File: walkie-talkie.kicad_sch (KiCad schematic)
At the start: 12 parts, among them J1 I2C, SW1 POWER, SW2 Transmit, U2 adafruit-MAX98357, U3 mems-mic

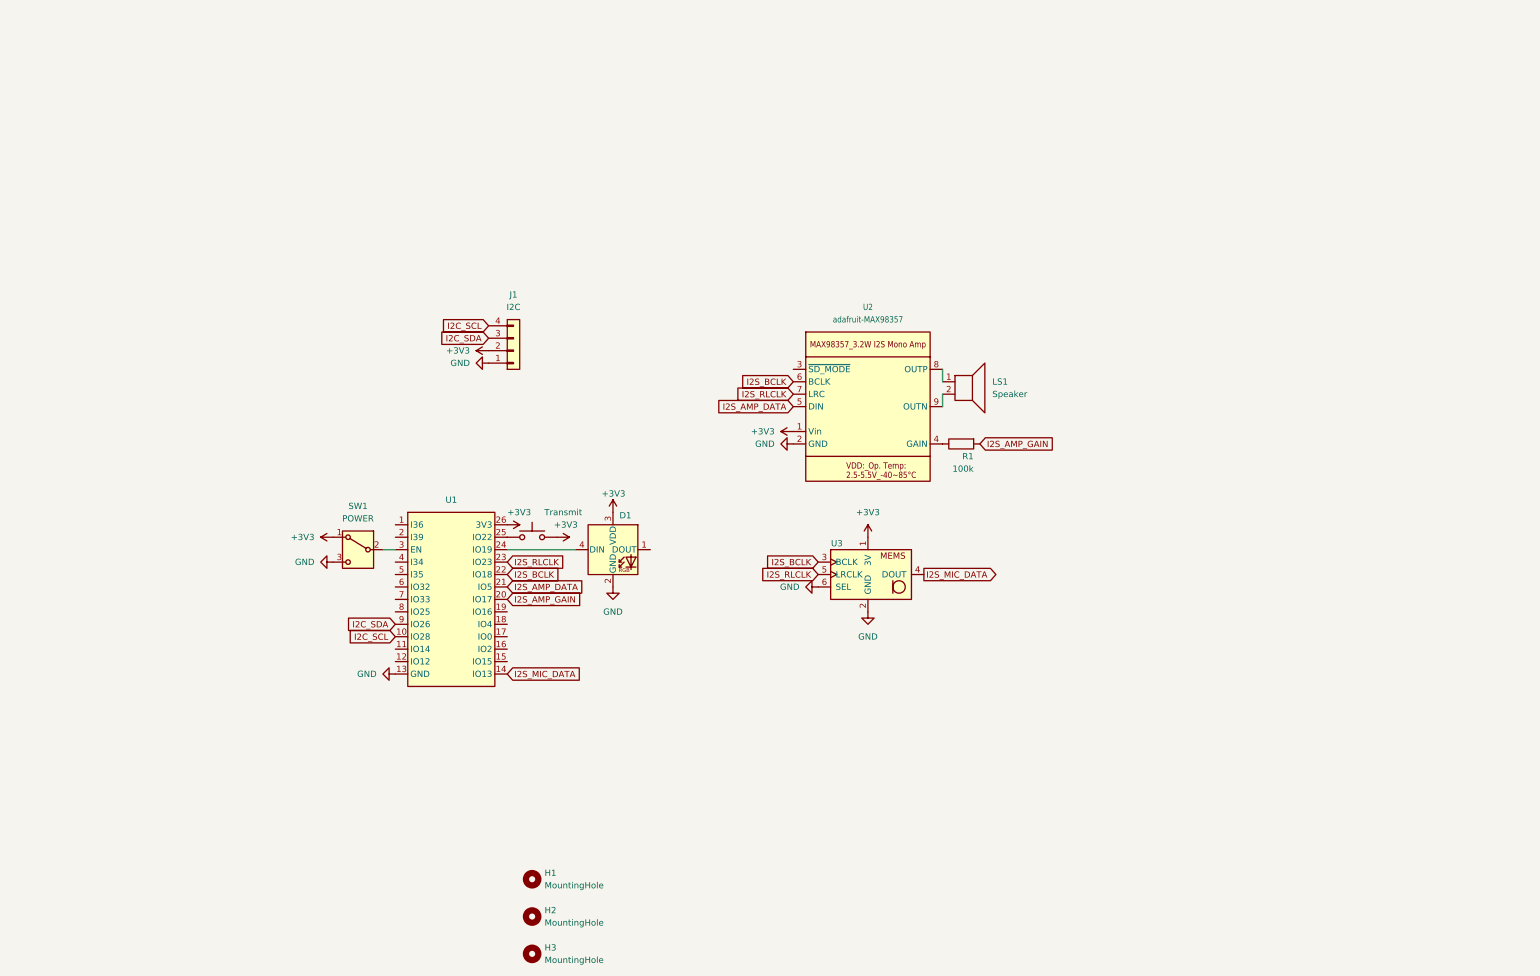
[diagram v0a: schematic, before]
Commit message: Add components for new PCB
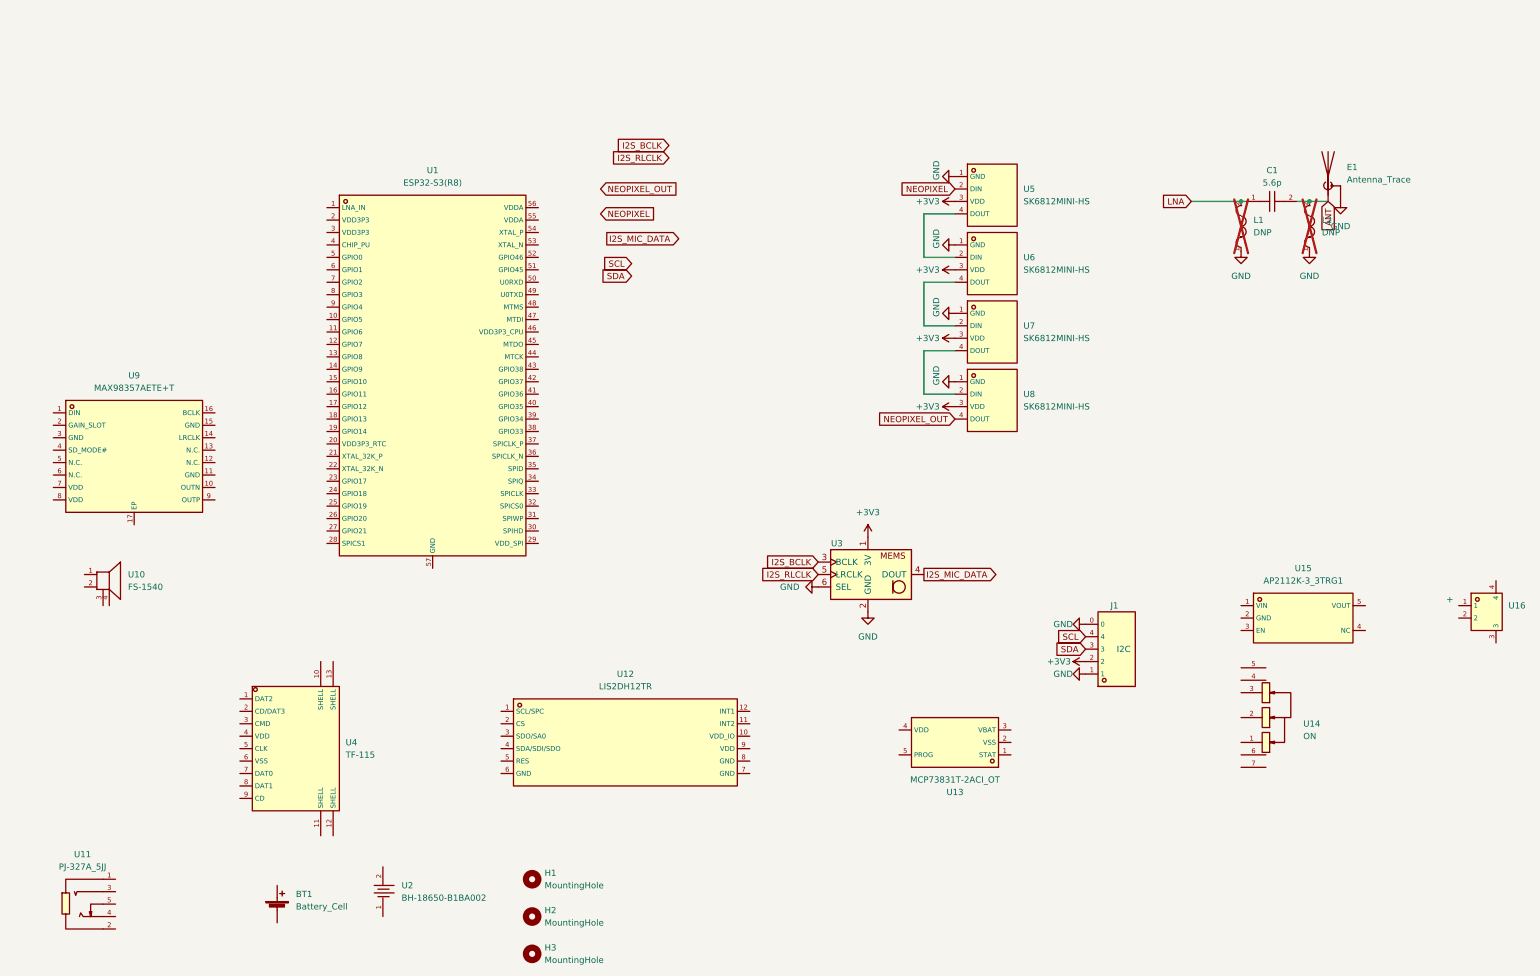
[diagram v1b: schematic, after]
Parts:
- removed D1: NeoPixel_THT, LED_THT:LED_D5.0mm-4_RGB_Wide_Pins, symbol LED:NeoPixel_THT
- removed J1: I2C, Connector_PinHeader_2.54mm:PinHeader_1x04_P2.54mm_Vertical, symbol Connector_Generic:Conn_01x04
- removed LS1: Speaker, Connector_PinSocket_2.54mm:PinSocket_1x04_P2.54mm_Horizontal, symbol Device:Speaker
- removed R1: 100k, Resistor_SMD:R_0805_2012Metric_Pad1.20x1.40mm_HandSolder, symbol Device:R
- removed SW1: POWER, Button_Switch_SMD:SW_SPDT_CK-JS102011SAQN, symbol Switch:SW_SPDT
- removed SW2: Transmit, pts636:pts636, symbol Switch:SW_Push
- removed U1: ~, lolin32-lite:lolin32-lite, symbol lolin32-lite:lolin32-lite
- removed U2: adafruit-MAX98357, adafruit-MAX98357:adafruit-MAX98357, symbol adafruit-MAX98357:adafruit-MAX98357
- added BT1: Battery_Cell, Battery:BatteryHolder_Keystone_2479_3xAAA, symbol Device:Battery_Cell
- added C1: 5.6p, jlc_footprints:C0603, symbol jlc_symbols:CC0603BRNPO9BN5R6
- added E1: Antenna_Trace, RF_Antenna:Texas_SWRA117D_2.4GHz_Right, symbol Device:Antenna_Shield
- added J1: I2C, footprint:CONN-SMD_BM04B-SRSS-TB, symbol BM04B-SRSS-TB(LF)(SN):BM04B-SRSS-TB(LF)(SN)
- added L1, L2: DNP, jlc_footprints:L0603, symbol jlc_symbols:SDFL1608S100KTF
- added U1: ESP32-S3(R8), jlc_footprints:QFN-56_L7.0-W7.0-P0.40-TL-EP4.0, symbol jlc_symbols:ESP32-S3(R8)
- added U10: FS-1540, jlc_footprints:BUZ-SMD_5P-L15.0-W15.0-P13.7-BL, symbol jlc_symbols:FS-1540
- added U11: PJ-327A_5JJ, jlc_footprints:AUDIO-SMD_PJ-327A5JJ, symbol jlc_symbols:PJ-327A_5JJ
- added U12: LIS2DH12TR, jlc_footprints:LGA-12_L2.0-W2.0-P0.50-BL, symbol jlc_symbols:LIS2DH12TR
- added U13: MCP73831T-2ACI_OT, jlc_footprints:SOT-23-5_L3.0-W1.7-P0.95-LS2.8-BL, symbol jlc_symbols:MCP73831T-2ACI_OT
- added U14: ON, jlc_footprints:SW-SMD_MK-12C02-G020, symbol jlc_symbols:MK-12C02-G020
- added U15: AP2112K-3_3TRG1, jlc_footprints:SOT-25-5_L2.9-W1.6-P0.95-LS2.8-BL, symbol jlc_symbols:AP2112K-3_3TRG1
- added U16: +, jlc_footprints:CONN-SMD_P2.00_S2B-PH-SM4-TB-LF-SN, symbol jlc_symbols:S2B-PH-SM4-TB(LF)(SN)
- added U2: BH-18650-B1BA002, jlc_footprints:BATTERY-SMD_18650-1S-L77.1-W20.7-1, symbol jlc_symbols:BH-18650-B1BA002
- added U4: TF-115, jlc_footprints:TF-SMD_TF-115, symbol jlc_symbols:TF-115
- added U5, U6, U7, U8: SK6812MINI-HS, jlc_footprints:LED-SMD_4P-L3.5-W3.5-BR_SK6812MINI-HS, symbol jlc_symbols:SK6812MINI-HS
- added U9: MAX98357AETE+T, jlc_footprints:TQFN-16_L3.0-W3.0-P0.50-BL-EP1.5, symbol jlc_symbols:MAX98357AETE+T
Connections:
- net +3V3: now also J1.2, U5.3 (VDD), U6.3 (VDD), U7.3 (VDD), U8.3 (VDD)
- net GND: now also E1.2 (Shield), J1.0, J1.1, L1.1, L2.1, U5.1 (GND), U6.1 (GND), U7.1 (GND), U8.1 (GND)
- new net: U5.4 (DOUT), U6.2 (DIN)
- new net: U6.4 (DOUT), U7.2 (DIN)
- new net: U7.4 (DOUT), U8.2 (DIN)
- new net ANT: C1.2, E1.1 (A), L2.2
- new net LNA: C1.1, L1.2
- new net NEOPIXEL: U5.2 (DIN)
- new net NEOPIXEL_OUT: U8.4 (DOUT)
- new net SCL: J1.4
- new net SDA: J1.3

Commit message: WIP
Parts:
- added JP1: USB_B_Micro, jlc_footprints:MICRO-USB-SMD_1050171001, symbol Connector:USB_B_Micro
- added U17: W25Q128JVSIQTR, jlc_footprints:SOIC-8_L5.3-W5.3-P1.27-LS8.0-BL, symbol jlc_symbols:W25Q128JVSIQTR
- added X1: X322540MPB4SI, jlc_footprints:OSC-SMD_4P-L3.2-W2.5-BL_SIT8008BI, symbol jlc_symbols:X322540MPB4SI
- H1, H2, H3: now left out of the parts list
- J1: footprint footprint:CONN-SMD_BM04B-SRSS-TB -> jlc_footprints:CONN-SMD_BM04B-SRSS-TB
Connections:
- net +3V3: now also U17.8 (VCC)
- net GND: now also JP1.5 (GND), JP1.6 (Shield), U17.4 (GND)
- net USB_N: now reaches U1.25 (GPIO19)
- net USB_N: now also JP1.2 (D-)
- net USB_P: now reaches U1.26 (GPIO20)
- net USB_P: now also JP1.3 (D+)
- new net SD_CLK: U17.6 (CLK)
- new net SD_CS0: U17.1 (CS#)
- new net SD_HD: U17.7 (IO3)
- new net SD_SI: U17.5 (DI)
- new net SD_SO: U17.2 (DO)
- new net SD_WP: U17.3 (IO2)
- new net VBUS: JP1.1 (VBUS)
- no-connect marks 0 -> 1
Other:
- note added: "GPIO0 needs pullup"
- note added: "GPIO3 needs to be floating"
- note added: "GPIO45 needs pull down"
- note added: "GPIO46 needs pull down"
- note added: "What capacitors for this crystal"
